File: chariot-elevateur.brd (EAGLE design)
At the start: 123 x 78 mm, 71 parts, among them CON1 XT-60, P1 RG500, Q1 DMN2056U, Q2 DMN2056U, U1 WIZ820IO

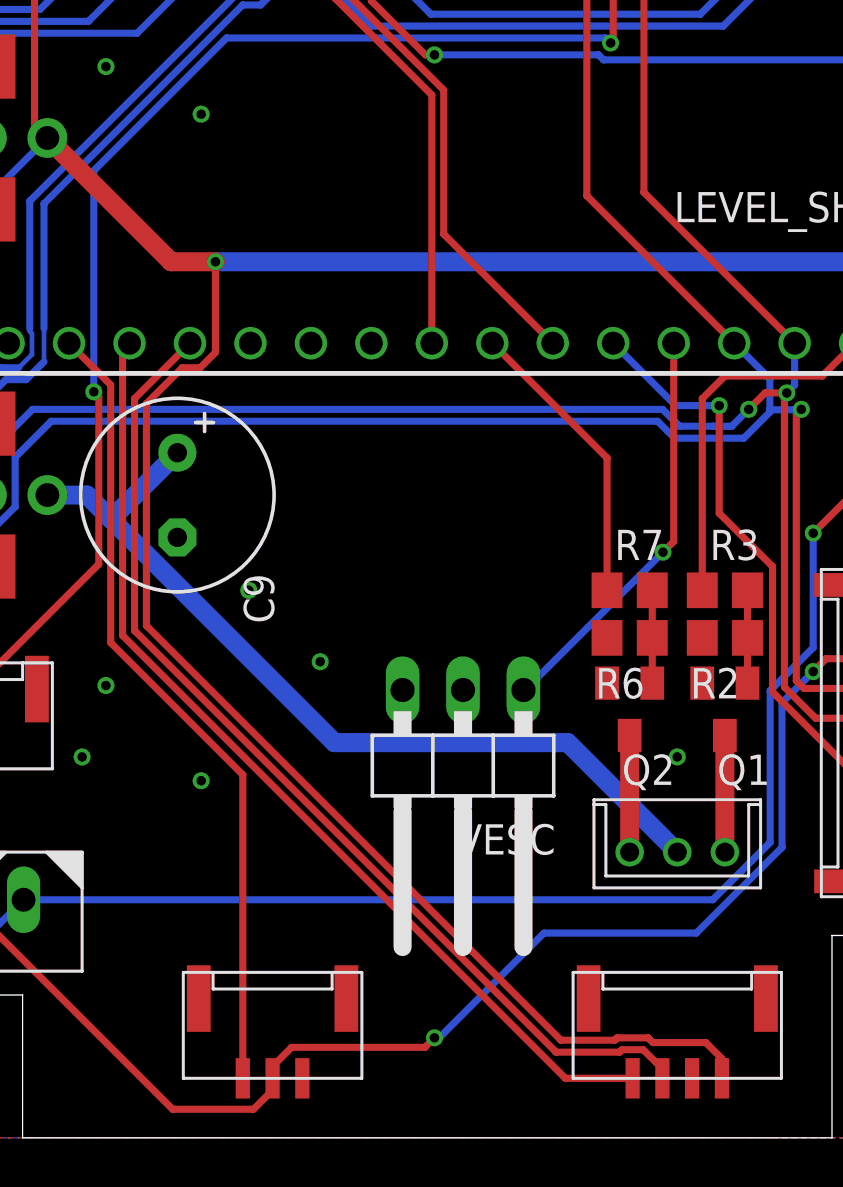
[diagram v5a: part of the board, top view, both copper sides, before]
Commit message: new file for rpi shield
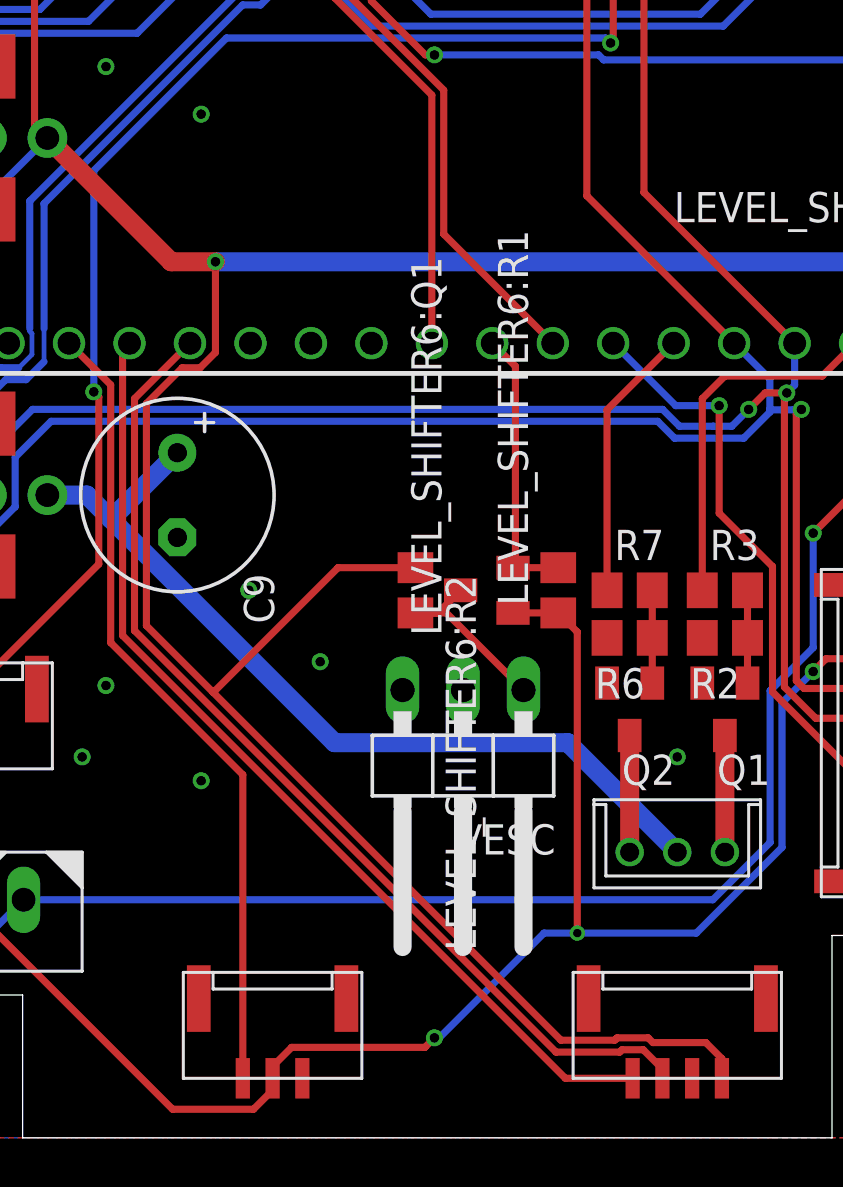
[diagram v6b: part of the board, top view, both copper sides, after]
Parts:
- added LEVEL_SHIFTER6:Q1: BSS138, transistor-small-signal:SOT23
- added LEVEL_SHIFTER6:R1, LEVEL_SHIFTER6:R2: 10k, resistor:R0805
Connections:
- new net VESC_CMD_5V: LEVEL_SHIFTER6:Q1.3, LEVEL_SHIFTER6:R2.2, VESC.1
- net +3V3: now also LEVEL_SHIFTER6:Q1.1, LEVEL_SHIFTER6:R1.1
- net +5V/1: now also LEVEL_SHIFTER6:R2.1
- net CMD_FUM_RES: now also TEENSY.17/A3; no longer TEENSY.14/A0
- net VESC_CMD: now also LEVEL_SHIFTER6:Q1.2, LEVEL_SHIFTER6:R1.2, TEENSY.14/A0; no longer TEENSY.17/A3, VESC.1
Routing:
- net +3V3: track 348.6 -> 364.2 mm, vias 5 -> 6
- net +5V/1: track 272.2 -> 282.8 mm
- net VESC_CMD_5V: track 0.00 -> 8.18 mm
- net VESC_CMD: track 17.2 -> 11.8 mm, vias 1 -> 0
- net CMD_FUM_RES: track 12.4 -> 11.5 mm
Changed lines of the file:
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@@
 <attribute name="VALUE" x="111.825" y="65.35" size="1.27" layer="27" rot="R270"/>
+</element>
+<element name="LEVEL_SHIFTER6:Q1" library="transistor-small-signal" library_urn="urn:adsk.eagle:library:401" package="SOT23" package3d_urn="urn:adsk.eagle:package:28738/2" value="BSS138" x="91" y="23" smashed="yes" rot="R90">
+<attribute name="NAME" x="89.095" y="21.095" size="1.27" layer="25" rot="R90"/>
+<attribute name="RS" value="669-7559" x="91" y="23" size="1.778" layer="27" rot="R90" display="off"/>
+<attribute name="VALUE" x="94.175" y="21.095" size="1.27" layer="27" rot="R90"/>
+</element>
+<element name="LEVEL_SHIFTER6:R1" library="resistor" library_urn="urn:adsk.eagle:library:348" package="R0805" package3d_urn="urn:adsk.eagle:package:23553/2" value="10k" x="94" y="23" smashed="yes" rot="R90">
+<attribute name="NAME" x="92.73" y="22.365" size="1.27" layer="25" rot="R90"/>
+<attribute name="VALUE" x="96.54" y="22.365" size="1.27" layer="27" rot="R90"/>
+</element>
+<element name="LEVEL_SHIFTER6:R2" library="resistor" library_urn="urn:adsk.eagle:library:348" package="R0805" package3d_urn="urn:adsk.eagle:package:23553/2" value="10k" x="88" y="23" smashed="yes" rot="R270">
+<attribute name="NAME" x="89.27" y="23.635" size="1.27" layer="25" rot="R270"/>
+<attribute name="VALUE" x="85.46" y="23.635" size="1.27" layer="27" rot="R270"/>
 </element>
 </elements>
@@
 <wire x1="88.8" y1="4.2" x2="88.4" y2="3.8" width="0.3" layer="1"/>
 <wire x1="82" y1="3" x2="82" y2="2.5" width="0.3" layer="1"/>
-<wire x1="99.8" y1="8.6" x2="93.4" y2="8.6" width="0.3" layer="16"/>
+<wire x1="99.8" y1="8.6" x2="94.8" y2="8.6" width="0.3" layer="16"/>
+<wire x1="94.8" y1="8.6" x2="93.4" y2="8.6" width="0.3" layer="16"/>
 <wire x1="93.4" y1="8.6" x2="89" y2="4.2" width="0.3" layer="16"/>
 <wire x1="88.4" y1="3.8" x2="82.8" y2="3.8" width="0.3" layer="1"/>
@@
 <wire x1="113.0574" y1="48.19228125" x2="113.0574" y2="57.0574" width="0.3" layer="1"/>
 <wire x1="113.0574" y1="57.0574" x2="115" y2="59" width="0.3" layer="1"/>
+<contactref element="LEVEL_SHIFTER6:Q1" pad="1"/>
+<contactref element="LEVEL_SHIFTER6:R1" pad="1"/>
+<wire x1="92.1" y1="22.05" x2="94" y2="22.05" width="0.3" layer="1"/>
+<wire x1="94" y1="22.05" x2="94.8" y2="21.25" width="0.3" layer="1"/>
+<wire x1="94.8" y1="21.25" x2="94.8" y2="8.6" width="0.3" layer="1"/>
+<via x="94.8" y="8.6" extent="1-16" drill="0.35"/>
 </signal>
 <signal name="CHOOSE_COLOR">
@@
 <wire x1="97.7770875" y1="4.2" x2="97.9770875" y2="4" width="0.3" layer="1"/>
 <wire x1="97.7770875" y1="4.2" x2="96.4729125" y2="4.2" width="0.3" layer="1"/>
-<wire x1="94.114225" y1="4.1" x2="76.7" y2="21.514225" width="0.3" layer="1"/>
+<wire x1="94.114225" y1="4.1" x2="79.5071125" y2="18.7071125" width="0.3" layer="1"/>
+<wire x1="79.5071125" y1="18.7071125" x2="76.7" y2="21.514225" width="0.3" layer="1"/>
 <wire x1="96.3729125" y1="4.1" x2="94.114225" y2="4.1" width="0.3" layer="1"/>
 <wire x1="76.7" y1="21.514225" x2="76.7" y2="30.8428875" width="0.3" layer="1"/>
@@
 <wire x1="118.8" y1="47.52968125" x2="118.1374" y2="48.19228125" width="0.3" layer="16"/>
 <wire x1="118.1374" y1="49.04771875" x2="118.8" y2="49.71031875" width="0.3" layer="16"/>
+<contactref element="LEVEL_SHIFTER6:R2" pad="1"/>
+<wire x1="88" y1="23.95" x2="84.75" y2="23.95" width="0.3" layer="1"/>
+<wire x1="84.75" y1="23.95" x2="79.5071125" y2="18.7071125" width="0.3" layer="1"/>
 </signal>
 <signal name="+5V/2" class="2">
@@
 </signal>
 <signal name="VESC_CMD">
-<contactref element="VESC" pad="1"/>
-<contactref element="TEENSY" pad="17/A3"/>
-<wire x1="98.85" y1="33.38" x2="98.85" y2="25.05" width="0.3" layer="1"/>
-<wire x1="98.85" y1="25.05" x2="98.4" y2="24.6" width="0.3" layer="1"/>
-<via x="98.4" y="24.6" extent="1-16" drill="0.4"/>
-<wire x1="98.4" y1="24.6" x2="92.61" y2="18.81" width="0.3" layer="16"/>
-<wire x1="92.61" y1="18.81" x2="92.54" y2="18.81" width="0.3" layer="16"/>
+<contactref element="LEVEL_SHIFTER6:R1" pad="2"/>
+<contactref element="LEVEL_SHIFTER6:Q1" pad="2"/>
+<wire x1="92.1" y1="23.95" x2="92.2" y2="24.05" width="0.3" layer="1"/>
+<wire x1="92.1" y1="23.95" x2="94" y2="23.95" width="0.3" layer="1"/>
+<contactref element="TEENSY" pad="14/A0"/>
+<wire x1="92.2" y1="32.41" x2="91.23" y2="33.38" width="0.3" layer="1"/>
+<wire x1="92.2" y1="24.05" x2="92.2" y2="32.41" width="0.3" layer="1"/>
 </signal>
 <signal name="JUMPER">
@@
 </signal>
 <signal name="CMD_FUM_RES">
-<contactref element="TEENSY" pad="14/A0"/>
 <contactref element="R7" pad="1"/>
-<wire x1="96.05" y1="23" x2="96.05" y2="28.56" width="0.3" layer="1"/>
-<wire x1="96.05" y1="28.56" x2="91.23" y2="33.38" width="0.3" layer="1"/>
+<contactref element="TEENSY" pad="17/A3"/>
+<wire x1="96.05" y1="30.58" x2="98.85" y2="33.38" width="0.3" layer="1"/>
+<wire x1="96.05" y1="23" x2="96.05" y2="30.58" width="0.3" layer="1"/>
 </signal>
 <signal name="CMD_DEL_AR">
@@
 <wire x1="102.27" y1="58" x2="105.05" y2="58" width="0.3" layer="1"/>
 </signal>
+<signal name="VESC_CMD_5V">
+<contactref element="LEVEL_SHIFTER6:Q1" pad="3"/>
+<contactref element="LEVEL_SHIFTER6:R2" pad="2"/>
+<contactref element="VESC" pad="1"/>
+<wire x1="88" y1="22.05" x2="88.95" y2="22.05" width="0.3" layer="1"/>
+<wire x1="88.95" y1="22.05" x2="89.9" y2="23" width="0.3" layer="1"/>
+<wire x1="92.54" y1="18.81" x2="89.3" y2="22.05" width="0.3" layer="1"/>
+<wire x1="89.3" y1="22.05" x2="88" y2="22.05" width="0.3" layer="1"/>
+</signal>
 </signals>

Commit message: add debug features
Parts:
- added 12V_AX12: (no value), pinhead:1X03
- added 5V_LED, 5V_SMOKE, 5V_TEENSY: (no value), pinhead:1X02
- added TP1, TP2, TP3: PTR1PAD1-13, testpad:P1-13
- moved LEVEL_SHIFTER3:R2 12.2 mm to (46.6, 18.6), turned to 90 degrees
- renumbered CON1 to LIPO, EXTRA to EXTRA1, USB to USB1
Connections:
- removed net N$9: DC4.3, SJ1.3
- new net REG_12V: 12V_AX12.1, DC4.3, SJ1.3
- net +12V: now also 12V_AX12.2
- net +5V/1: now also 5V_TEENSY.1, LEVEL_SHIFTER2:R2.1, LEVEL_SHIFTER3:R2.1
- net +5V/2: now also 5V_LED.1; no longer LEVEL_SHIFTER2:R2.1, LEVEL_SHIFTER3:R2.1
- net +5V/3: now also 5V_SMOKE.1
- net CMD_DEL_AR_5V: now also TP2.TP
- net CMD_DEL_AV_5V: now also TP1.TP
- net GND: now also 12V_AX12.3, 5V_LED.2, 5V_SMOKE.2, 5V_TEENSY.2
- net SERIAL_AX12_5V: now also TP3.TP
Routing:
- net +5V/1: track 282.8 -> 362.7 mm
- net REG_12V: track 0.00 -> 9.44 mm
- net CMD_DEL_AR_5V: track 11.2 -> 18.9 mm
- net +5V/3: track 36.6 -> 43.7 mm
- net SERIAL_AX12_5V: track 142.8 -> 149.3 mm
- net N$9: track 4.94 -> 0.00 mm
- net +5V/2: track 69.6 -> 64.8 mm
- net +12V: track 86.4 -> 90.4 mm
- net CMD_DEL_AV_5V: track 6.14 -> 9.16 mm
- net GND: vias 35 -> 40

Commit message: all done, missing doc
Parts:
- removed 5V_TEENSY: (no value), pinhead:1X02
- added FUMIGENE1: DYNAMIXEL-1X03XL, 1NTech_pinhead:DYNAMIXEL_XL_1X03
- added Q3, Q4: DMN2056U, transistor-small-signal:SOT23
- added R10, R12: 10k, resistor:R0805
- added R11, R13: 100, resistor:R0805
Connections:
- new net EXTRA_POWER_SWITCH_1: FUMIGENE1.GND, Q3.3
- new net EXTRA_POWER_SWITCH_2: FUMIGENE1.DATA, Q4.3
- new net N$12: Q4.1, R12.1, R13.2
- new net N$9: Q3.1, R10.1, R11.2
- net +5V/1: no longer 5V_TEENSY.1
- net +5V/3: now also FUMIGENE1.VCC
- net EXTRA_GPIO_1: now also R11.1
- net EXTRA_GPIO_2: now also R13.1
- net GND: now also Q3.2, Q4.2, R10.2, R12.2; no longer 5V_TEENSY.2
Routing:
- net +5V/3: track 43.7 -> 79.9 mm
- net EXTRA_GPIO_1: track 9.68 -> 31.0 mm, vias 0 -> 1
- net EXTRA_GPIO_2: track 6.73 -> 26.8 mm, vias 0 -> 1
- net +5V/1: track 362.7 -> 358.3 mm
- net N$9: track 0.00 -> 3.90 mm
- net N$12: track 0.00 -> 3.90 mm
- net EXTRA_POWER_SWITCH_2: track 0.00 -> 3.40 mm
- net EXTRA_POWER_SWITCH_1: track 0.00 -> 3.40 mm
- net GND: vias 40 -> 42
